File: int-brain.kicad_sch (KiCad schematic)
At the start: 52 parts, among them J1 PWR, J10 Left, J11 Right, J12 1MA_ENC, J13 1MB_ENC, J14 2MA_ENC, J15 2MB_ENC, J16 USB_A, J2 UART0, J3 I2C0, J4 PWR, J5 1MA, J6 1MB, J7 2MA, J8 2MB, J9 MPU9250, SW1 SW_Push, U2 ESP32-DevKitC, U7 PCA9635

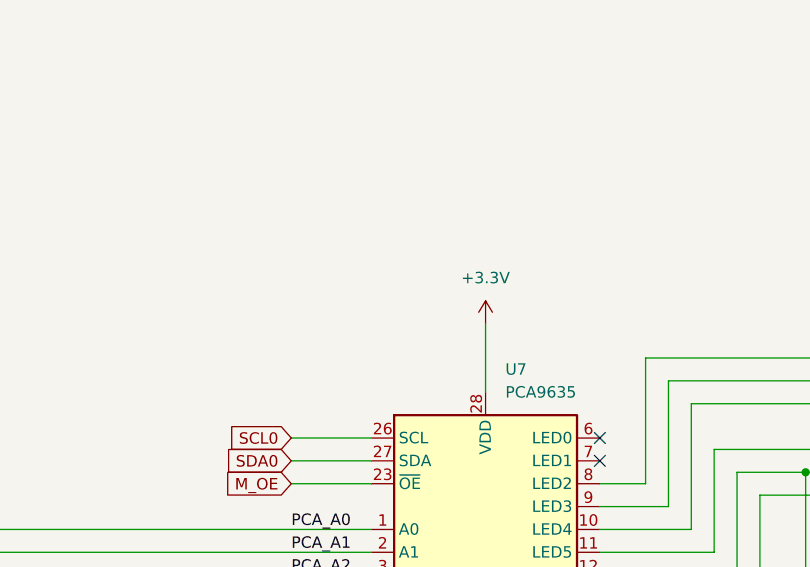
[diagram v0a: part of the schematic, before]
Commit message: add cap to PCA ic
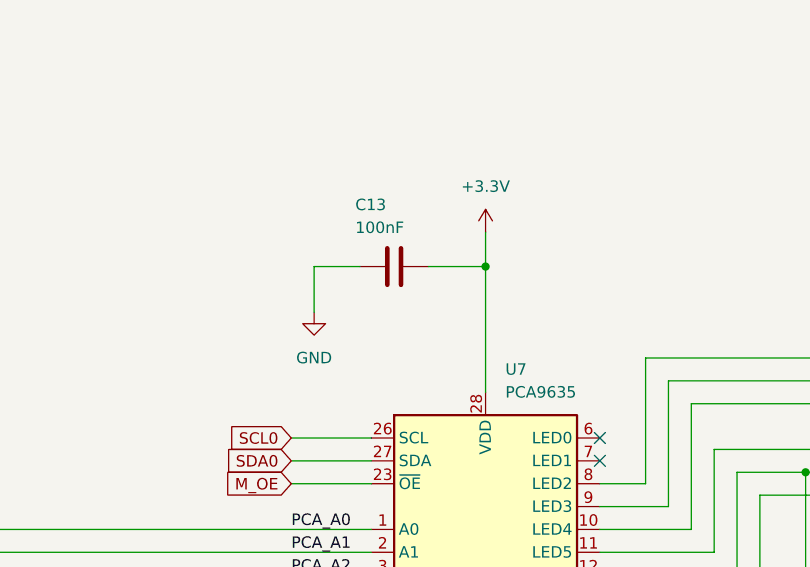
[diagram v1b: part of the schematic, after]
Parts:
- added C13: 100nF, Capacitor_SMD:C_0603_1608Metric_Pad1.08x0.95mm_HandSolder, symbol Device:C
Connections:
- net +3.3V: now also C13.1
- net GND: now also C13.2
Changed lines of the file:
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@@
 	)
 	(junction
+		(at 151.13 354.33)
+		(diameter 0)
+		(color 0 0 0 0)
+	)
+	(junction
 		(at 95.25 408.94)
 		(diameter 0)
@@
 	(wire
 		(pts
+			(xy 132.08 354.33) (xy 132.08 359.41)
+		)
+		(stroke
+			(width 0)
+			(type default)
+		)
+	)
+	(wire
+		(pts
 			(xy 328.93 158.75) (xy 328.93 146.05)
 		)
@@
 	(wire
 		(pts
+			(xy 137.16 354.33) (xy 132.08 354.33)
+		)
+		(stroke
+			(width 0)
+			(type default)
+		)
+	)
+	(wire
+		(pts
 			(xy 95.25 408.94) (xy 105.41 408.94)
 		)
@@
 	(wire
 		(pts
+			(xy 151.13 354.33) (xy 151.13 368.3)
+		)
+		(stroke
+			(width 0)
+			(type default)
+		)
+	)
+	(wire
+		(pts
 			(xy 81.28 224.79) (xy 81.28 271.78)
 		)
@@
 	(wire
 		(pts
+			(xy 144.78 354.33) (xy 151.13 354.33)
+		)
+		(stroke
+			(width 0)
+			(type default)
+		)
+	)
+	(wire
+		(pts
 			(xy 38.1 367.03) (xy 40.64 367.03)
 		)
@@
 	(wire
 		(pts
-			(xy 151.13 360.68) (xy 151.13 368.3)
+			(xy 151.13 350.52) (xy 151.13 354.33)
 		)
 		(stroke
@@
 	)
 	(symbol
+		(lib_id "Device:C")
+		(at 140.97 354.33 270)
+		(unit 1)
+		(exclude_from_sim no)
+		(in_bom yes)
+		(on_board yes)
+		(dnp no)
+		(property "Reference" "C13"
+			(at 136.652 347.472 90)
+			(effects
+				(font
+					(size 1.27 1.27)
+				)
+				(justify left)
+			)
+		)
+		(property "Value" "100nF"
+			(at 136.652 350.012 90)
+			(effects
+				(font
+					(size 1.27 1.27)
+				)
+				(justify left)
+			)
+		)
+		(property "Footprint" "Capacitor_SMD:C_0603_1608Metric_Pad1.08x0.95mm_HandSolder"
+			(at 137.16 355.2952 0)
+			(effects
+				(font
+					(size 1.27 1.27)
+				)
+				(hide yes)
+			)
+		)
+		(property "Datasheet" "~"
+			(at 140.97 354.33 0)
+			(effects
+				(font
+					(size 1.27 1.27)
+				)
+				(hide yes)
+			)
+		)
+		(property "Description" "Unpolarized capacitor"
+			(at 140.97 354.33 0)
+			(effects
+				(font
+					(size 1.27 1.27)
+				)
+				(hide yes)
+			)
+		)
+		(pin "2"
+		)
+		(pin "1"
+		)
+		(instances
+			(project "int-brain"
+				(path "/177c6115-ec2a-43b1-88e2-eca3e5dd1279"
+					(reference "C13")
+					(unit 1)
+				)
+			)
+		)
+	)
+	(symbol
 		(lib_id "Jumper:SolderJumper_2_Open")
 		(at 44.45 393.7 0)
@@
 	)
 	(symbol
+		(lib_id "power:GND")
+		(at 132.08 359.41 0)
+		(unit 1)
+		(exclude_from_sim no)
+		(in_bom yes)
+		(on_board yes)
+		(dnp no)
+		(fields_autoplaced yes)
+		(property "Reference" "#PWR030"
+			(at 132.08 365.76 0)
+			(effects
+				(font
+					(size 1.27 1.27)
+				)
+				(hide yes)
+			)
+		)
+		(property "Value" "GND"
+			(at 132.08 364.49 0)
+			(effects
+				(font
+					(size 1.27 1.27)
+				)
+			)
+		)
+		(property "Footprint" ""
+			(at 132.08 359.41 0)
+			(effects
+				(font
+					(size 1.27 1.27)
+				)
+				(hide yes)
+			)
+		)
+		(property "Datasheet" ""
+			(at 132.08 359.41 0)
+			(effects
+				(font
+					(size 1.27 1.27)
+				)
+				(hide yes)
+			)
+		)
+		(property "Description" "Power symbol creates a global label with name \"GND\" , ground"
+			(at 132.08 359.41 0)
+			(effects
+				(font
+					(size 1.27 1.27)
+				)
+				(hide yes)
+			)
+		)
+		(pin "1"
+		)
+		(instances
+			(project "int-brain"
+				(path "/177c6115-ec2a-43b1-88e2-eca3e5dd1279"
+					(reference "#PWR030")
+					(unit 1)
+				)
+			)
+		)
+	)
+	(symbol
 		(lib_id "power:+3.3V")
-		(at 151.13 360.68 0)
+		(at 151.13 350.52 0)
 		(unit 1)
 		(exclude_from_sim no)
@@
 		(fields_autoplaced yes)
 		(property "Reference" "#PWR039"
-			(at 151.13 364.49 0)
+			(at 151.13 354.33 0)
 			(effects
 				(font
@@
 		)
 		(property "Value" "+3.3V"
-			(at 151.13 355.6 0)
+			(at 151.13 345.44 0)
 			(effects
 				(font
@@
 		)
 		(property "Footprint" ""
-			(at 151.13 360.68 0)
+			(at 151.13 350.52 0)
 			(effects
 				(font
@@
 		)
 		(property "Datasheet" ""
-			(at 151.13 360.68 0)
+			(at 151.13 350.52 0)
 			(effects
 				(font
@@
 		)
 		(property "Description" "Power symbol creates a global label with name \"+3.3V\""
-			(at 151.13 360.68 0)
+			(at 151.13 350.52 0)
 			(effects
 				(font

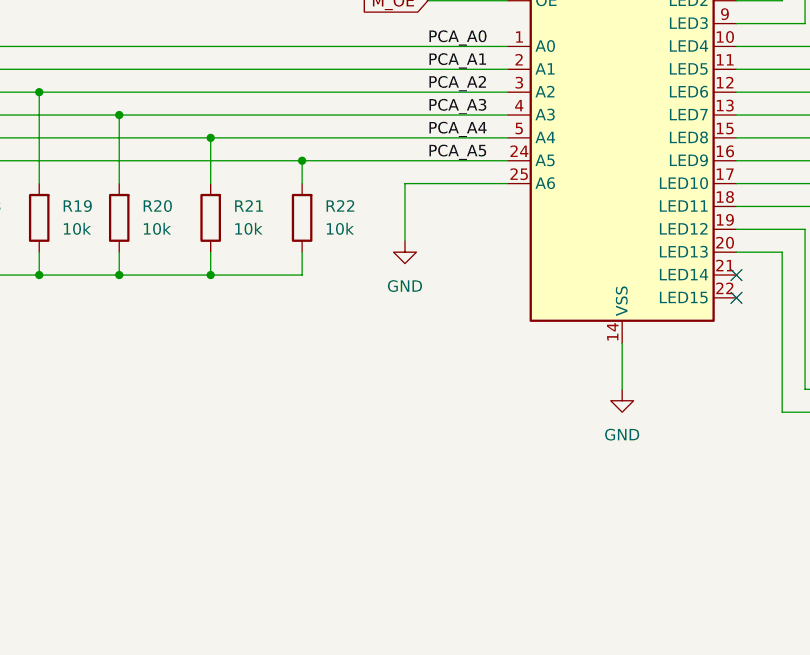
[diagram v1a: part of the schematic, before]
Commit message: add solder point for PCA I/O
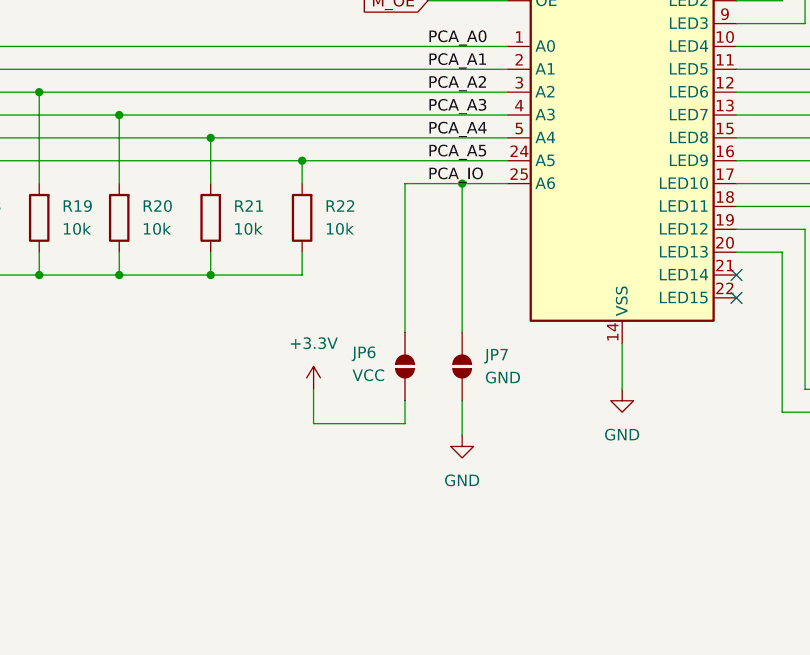
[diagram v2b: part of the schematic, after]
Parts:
- added JP6: VCC, Jumper:SolderJumper-2_P1.3mm_Open_Pad1.0x1.5mm, symbol Jumper:SolderJumper_2_Open
- added JP7: GND, Jumper:SolderJumper-2_P1.3mm_Open_Pad1.0x1.5mm, symbol Jumper:SolderJumper_2_Open
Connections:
- net +3.3V: now also JP6.1 (A)
- net GND: now also JP7.1 (A); no longer U7.25 (A6)
- new net PCA_IO: JP6.2 (B), JP7.2 (B), U7.25 (A6)

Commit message: placed?
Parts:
- removed JP7: GND, Jumper:SolderJumper-2_P1.3mm_Open_Pad1.0x1.5mm, symbol Jumper:SolderJumper_2_Open
- added D10: D, Diode_SMD:D_SMA_Handsoldering, symbol Device:D
- added J17: Conn_01x03, Connector_PinHeader_2.54mm:PinHeader_1x03_P2.54mm_Vertical, symbol Connector_Generic:Conn_01x03
- added R29: 10k, Resistor_SMD:R_1206_3216Metric_Pad1.30x1.75mm_HandSolder, symbol Device:R
- added R30: 3k9, Resistor_SMD:R_1206_3216Metric_Pad1.30x1.75mm_HandSolder, symbol Device:R
- D1: renamed from D18; footprint LED_SMD:LED_0603_1608Metric_Pad1.05x0.95mm_HandSolder -> LED_SMD:LED_1206_3216Metric_Pad1.42x1.75mm_HandSolder
- D2: renamed from D19; footprint LED_SMD:LED_0603_1608Metric_Pad1.05x0.95mm_HandSolder -> LED_SMD:LED_1206_3216Metric_Pad1.42x1.75mm_HandSolder
- D3: renamed from D20; footprint LED_SMD:LED_0603_1608Metric_Pad1.05x0.95mm_HandSolder -> LED_SMD:LED_1206_3216Metric_Pad1.42x1.75mm_HandSolder
- D4: renamed from D21; footprint LED_SMD:LED_0603_1608Metric_Pad1.05x0.95mm_HandSolder -> LED_SMD:LED_1206_3216Metric_Pad1.42x1.75mm_HandSolder
- D6: renamed from D25; footprint LED_SMD:LED_0603_1608Metric_Pad1.05x0.95mm_HandSolder -> LED_SMD:LED_1206_3216Metric_Pad1.42x1.75mm_HandSolder
- D7: renamed from D22; footprint LED_SMD:LED_0603_1608Metric_Pad1.05x0.95mm_HandSolder -> LED_SMD:LED_1206_3216Metric_Pad1.42x1.75mm_HandSolder
- R10: renamed from R11; value 10k -> 3k9
- U2: footprint PCM_Espressif:ESP32-DevKitC -> PCM_Espressif:ESP32-DevKitC-slim
- renumbered C13 to C1, D23 to D5, J11 to J1, J8 to J10, J6 to J11, J5 to J12, J12 to J13, J13 to J14, J14 to J15, J9 to J16, J10 to J2, J1 to J3, J16 to J5, J15 to J6, J3 to J7, J2 to J8, J7 to J9, JP0 to JP1, JP1 to JP2, JP2 to JP3, JP3 to JP4, JP4 to JP5, JP5 to JP6, JP6 to JP7, R5 to R1, R21 to R11, R22 to R12, R23 to R13, R9 to R14, R16 to R15, R17 to R16, R6 to R2, R7 to R3, R28 to R4, R8 to R5, R18 to R6, R19 to R7, R10 to R8, R20 to R9, U7 to U1
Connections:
- net 1MA_EN: now also U1.22 (LED15); no longer U1.12 (LED6)
- net 1MB_EN: now also U1.21 (LED14); no longer U1.9 (LED3)
- net 2MA_EN: now also U1.6 (LED0); no longer U1.16 (LED9)
- net 2MB_EN: now also U1.7 (LED1); no longer U1.19 (LED12)
- net BUCK_VS: no longer D5.1 (K)
- net GND: now also J3.3 (MountPin), R29.1, R30.2; no longer J3.MP (MountPin)
- net PCA_IO: now also R29.2
- net VBATT: now also J17.2 (Pin_2); no longer R10.1
- net VS: now also D5.1 (K), D10.1 (K); no longer D5.2 (A), J3.1, J4.2 (Pin_2)
- net 1MA1_IN renamed 2MB_IN2
- net 1MA2_IN renamed 2MA_IN2
- net 1MB1_IN renamed 2MA_IN1
- net 1MB2_IN: no longer names the net of U1.8 (LED2)
- net 2MA1_IN renamed 1MB_IN1
- net 2MA2_IN renamed 1MA_IN1
- net 2MB1_IN renamed 1MA_IN2
- net 2MB2_IN: no longer names the net of U1.20 (LED13)
- new net 1MB_IN2: U1.16 (LED9)
- new net 2MB_IN1: U1.12 (LED6)
- new net 3S: J17.3 (Pin_3), R10.1
- new net 6S: J17.1 (Pin_1), R30.1
- new net VS_UNSAFE: D10.2 (A), D5.2 (A), J3.1, J4.2 (Pin_2)
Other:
- removed sheet motor_driver_1
- removed sheet motor_driver_2
- added sheet motor-driver-1 (motor-driver-DRV8251A.kicad_sch)
- added sheet motor-driver-2 (motor-driver-DRV8251A.kicad_sch)
- added sheet motor-driver-3 (motor-driver-DRV8251A.kicad_sch)
- added sheet motor-driver-4 (motor-driver-DRV8251A.kicad_sch)
- moved on the sheet: D1, D2, D3, D4, D5, J10, J11, J12, J3, J4, J9, R1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

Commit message: traced
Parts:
- added C26, C27: 10uF, Capacitor_SMD:C_1206_3216Metric_Pad1.33x1.80mm_HandSolder, symbol Device:C
- added U13: AMS1117-3.3, Package_TO_SOT_SMD:SOT-223-3_TabPin2, symbol Regulator_Linear:AMS1117-3.3
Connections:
- net BUCK_VS is gone; now on net VS: SW1.1
- net GPIO32 is gone; now on net FSYNC: J2.7 (Pin_7), U2.7 (32K_XP/GPIO32/ADC1_CH4)
- net GPIO33 is gone; now on net INT: J2.8 (Pin_8), U2.8 (32K_XN/GPIO33/ADC1_CH5)
- net +3.3V: now also C27.1, U13.2 (VO); no longer J2.1 (Pin_1), U2.1 (3V3)
- net 1MA1_ENC: now also J1.9 (Pin_9), U2.30 (GPIO18); no longer J1.11 (Pin_11), U2.28 (GPIO17)
- net 1MA2_ENC: now also J1.8 (Pin_8), U2.31 (GPIO19); no longer J1.10 (Pin_10), U2.29 (GPIO5)
- net 1MA_EN: now also U1.18 (LED11); no longer U1.22 (LED15)
- net 1MA_IN1: now also U1.19 (LED12); no longer U1.17 (LED10)
- net 1MA_IN2: now also U1.20 (LED13); no longer U1.18 (LED11)
- net 1MB1_ENC: now also J2.11 (Pin_11), U2.11 (ADC2_CH7/GPIO27); no longer J2.12 (Pin_12), U2.12 (MTMS/GPIO14/ADC2_CH6)
- net 1MB2_ENC: now also J2.10 (Pin_10), U2.10 (DAC_2/ADC2_CH9/GPIO26); no longer J2.13 (Pin_13), U2.13 (MTDI/GPIO12/ADC2_CH5)
- net 1MB_EN: now also U1.17 (LED10); no longer U1.21 (LED14)
- net 2MA1_ENC: now also J1.10 (Pin_10), U2.29 (GPIO5); no longer J1.8 (Pin_8), U2.31 (GPIO19)
- net 2MA2_ENC: now also J1.11 (Pin_11), U2.28 (GPIO17); no longer J1.9 (Pin_9), U2.30 (GPIO18)
- net 2MA_EN: now also U1.8 (LED2); no longer U1.6 (LED0)
- net 2MA_IN1: now also U1.9 (LED3); no longer U1.10 (LED4)
- net 2MA_IN2: now also U1.10 (LED4); no longer U1.11 (LED5)
- net 2MB1_ENC: now also J2.12 (Pin_12), U2.12 (MTMS/GPIO14/ADC2_CH6); no longer J2.10 (Pin_10), U2.10 (DAC_2/ADC2_CH9/GPIO26)
- net 2MB2_ENC: now also J2.13 (Pin_13), U2.13 (MTDI/GPIO12/ADC2_CH5); no longer J2.11 (Pin_11), U2.11 (ADC2_CH7/GPIO27)
- net 2MB_EN: now also U1.13 (LED7); no longer U1.7 (LED1)
- net 2MB_IN1: now also U1.11 (LED5); no longer U1.12 (LED6)
- net 2MB_IN2: now also U1.12 (LED6); no longer U1.13 (LED7)
- net FSYNC: no longer J1.2 (Pin_2), U2.37 (GPIO23)
- net GND: now also C26.2, C27.2, U13.1 (GND)
- net INT: no longer J1.12 (Pin_12), U2.27 (GPIO16)
- net VSS: now also C26.1, U13.3 (VI)
- new net +3.3VA: J2.1 (Pin_1), U2.1 (3V3)
- new net GPIO16: J1.12 (Pin_12), U2.27 (GPIO16)
- new net GPIO23: J1.2 (Pin_2), U2.37 (GPIO23)
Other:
- moved on the sheet: J15, J6

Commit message: done?
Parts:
- added R31: 10k, Resistor_SMD:R_1206_3216Metric_Pad1.30x1.75mm_HandSolder, symbol Device:R
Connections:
- net +3.3V: now also R31.2
- net M_OE: now also R31.1
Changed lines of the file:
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@@
 	)
 	(junction
+		(at 114.3 354.33)
+		(diameter 0)
+		(color 0 0 0 0)
+	)
+	(junction
 		(at 132.08 463.55)
 		(diameter 0)
@@
 	(wire
 		(pts
+			(xy 114.3 354.33) (xy 114.3 378.46)
+		)
+		(stroke
+			(width 0)
+			(type default)
+		)
+	)
+	(wire
+		(pts
 			(xy 298.45 439.42) (xy 317.5 439.42)
 		)
@@
 	(wire
 		(pts
+			(xy 114.3 336.55) (xy 114.3 342.9)
+		)
+		(stroke
+			(width 0)
+			(type default)
+		)
+	)
+	(wire
+		(pts
 			(xy 50.8 209.55) (xy 97.79 209.55)
 		)
@@
 	(wire
 		(pts
+			(xy 114.3 350.52) (xy 114.3 354.33)
+		)
+		(stroke
+			(width 0)
+			(type default)
+		)
+	)
+	(wire
+		(pts
 			(xy 328.93 163.83) (xy 328.93 158.75)
 		)
@@
 	(wire
 		(pts
-			(xy 129.54 378.46) (xy 138.43 378.46)
+			(xy 105.41 354.33) (xy 114.3 354.33)
 		)
 		(stroke
@@
 	(wire
 		(pts
+			(xy 114.3 378.46) (xy 138.43 378.46)
+		)
+		(stroke
+			(width 0)
+			(type default)
+		)
+	)
+	(wire
+		(pts
 			(xy 322.58 143.51) (xy 322.58 156.21)
 		)
@@
 	(global_label "M_OE"
 		(shape input)
-		(at 129.54 378.46 180)
+		(at 105.41 354.33 180)
 		(fields_autoplaced yes)
 		(effects
@@
 		)
 		(property "Intersheetrefs" "${INTERSHEET_REFS}"
-			(at 121.6563 378.46 0)
+			(at 97.5263 354.33 0)
 			(effects
 				(font
@@
 	)
 	(symbol
+		(lib_id "power:+3.3V")
+		(at 114.3 336.55 0)
+		(unit 1)
+		(exclude_from_sim no)
+		(in_bom yes)
+		(on_board yes)
+		(dnp no)
+		(fields_autoplaced yes)
+		(property "Reference" "#PWR059"
+			(at 114.3 340.36 0)
+			(effects
+				(font
+					(size 1.27 1.27)
+				)
+				(hide yes)
+			)
+		)
+		(property "Value" "+3.3V"
+			(at 114.3 331.47 0)
+			(effects
+				(font
+					(size 1.27 1.27)
+				)
+			)
+		)
+		(property "Footprint" ""
+			(at 114.3 336.55 0)
+			(effects
+				(font
+					(size 1.27 1.27)
+				)
+				(hide yes)
+			)
+		)
+		(property "Datasheet" ""
+			(at 114.3 336.55 0)
+			(effects
+				(font
+					(size 1.27 1.27)
+				)
+				(hide yes)
+			)
+		)
+		(property "Description" "Power symbol creates a global label with name \"+3.3V\""
+			(at 114.3 336.55 0)
+			(effects
+				(font
+					(size 1.27 1.27)
+				)
+				(hide yes)
+			)
+		)
+		(pin "1"
+		)
+		(instances
+			(project "int-brain"
+				(path "/177c6115-ec2a-43b1-88e2-eca3e5dd1279"
+					(reference "#PWR059")
+					(unit 1)
+				)
+			)
+		)
+	)
+	(symbol
 		(lib_id "Jumper:SolderJumper_2_Open")
 		(at 44.45 375.92 0)
@@
 					(unit 1)
 				)
+			)
+		)
+	)
+	(symbol
+		(lib_id "Device:R")
+		(at 114.3 346.71 180)
+		(unit 1)
+		(exclude_from_sim no)
+		(in_bom yes)
+		(on_board yes)
+		(dnp no)
+		(fields_autoplaced yes)
+		(property "Reference" "R31"
+			(at 116.84 345.4399 0)
+			(effects
+				(font
+					(size 1.27 1.27)
+				)
+				(justify right)
+			)
+		)
+		(property "Value" "10k"
+			(at 116.84 347.9799 0)
+			(effects
+				(font
+					(size 1.27 1.27)
+				)
+				(justify right)
+			)
+		)
+		(property "Footprint" "Resistor_SMD:R_1206_3216Metric_Pad1.30x1.75mm_HandSolder"
+			(at 116.078 346.71 90)
+			(effects
+				(font
+					(size 1.27 1.27)
+				)
+				(hide yes)
+			)
+		)
+		(property "Datasheet" "~"
+			(at 114.3 346.71 0)
+			(effects
+				(font
+					(size 1.27 1.27)
+				)
+				(hide yes)
+			)
+		)
+		(property "Description" "Resistor"
+			(at 114.3 346.71 0)
+			(effects
+				(font
+					(size 1.27 1.27)
+				)
+				(hide yes)
+			)
+		)
+		(pin "2"
+		)
+		(pin "1"
+		)
+		(instances
+			(project "int-brain"
+				(path "/177c6115-ec2a-43b1-88e2-eca3e5dd1279"
+					(reference "R31")
+					(unit 1)
+				)

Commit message: minor improvements
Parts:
- D10, D5: value D -> M7
- J1: value Right -> Top
- J17: value Conn_01x03 -> VBATT_SELECT
- J2: value Left -> Bottom
- JP7: value VCC -> I/O
- R30: value 3k9 -> 2k
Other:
- note added: "3.3V LDO"
- note added: "Default I/O to output mode by pull-down."
- note added: "Distriute functionality from the ESP32 to the rest of the board. In general, the signal bus is used to connect headers on either side of the board to access its GPIO and other functionality. Nothing else on the board depends on ESP32 3.3V, so this can be used for peripherals."
- note added: "Drive all motors using PWM signals, sent from the ESP32 using I2C. Eachmotor requires two PWM lines, each corresponding to one pair of the MOSFETs in the H-bridge motor driver. An additional PWM pin has been allocated per motor to indicate speed with LED brightness."
- note added: "ESP32 Microcontroller"
- note added: "I2C address selection is done by pulling down all bits to 0 using a 10k resistor to ground. To make any of them 1, the corresponding solder joint can be filled, and they'll be shorted to 3.3 V."
- note added: "MPU9250 Datasheet: https://invensense.tdk.com/wp-content/uploads/2015/02/ PS-MPU-9250A-01-v1.1.pdf"
- note added: "Motor Logic Section"
- note added: "Note that this +3.3VA is different from the +3.3V used in the rest of the circuit. This is to ensure that the 3.3 V required for the ESP32 is left undisturbed and other components are powered using a dedicated AMS1117-3.3 LDO."
- note added: "PCA9635 datasheet: https://www.nxp.com/docs/en/data-sheet/PCA9635.pdf"
- note added: "Pinout and other information: https://docs.espressif.com/projects/esp-idf/en/stable/esp32/ hw-reference/esp32/get-started-devkitc.html"
- note added: "Power Input Section"
- note added: "Protocol pins (I2C and UART0) are chosen to keep compliance with the Arduino framework, even though this is unlikely to be used with this board. Most other GPIO are chosen based on physical proximity to peripherals and ease of routing the PCB."
- note added: "Provide up to 5V 5A at a USB port, used to drive an SBC such as the Raspberry Pi 5B"
- note added: "SBC Power section"
- note added: "Sensor Module product links - https://robu.in/product/gy-9255-mpu9255-sensor-module/ - https://www.electronicscomp.com/mpu9250-9-axis-gyro- accelerometer-module - https://www.amazon.in/Electrobot-MPU9250-Accelerator- Magnetometer-Arduino/dp/B08R3SXRVH - https://roboticsdna.in/product/gy-87-mpu-9265-3-axis-9-dof- attitude-gyro-magnetometer-accelerator-sensor-module/ - https://rees52.com/products/m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"
- note added: "Support for quadrature rotary encoders is added, in case a compatible motor with encoders can be found. These are connected directly to the ESP32 microcontroller (instead of using another PCA PWM driver) to provide easy configration of hardware interrupts in case this approach is used when programming for the encoders. One JST header for each encoder (one per motor)."
- note added: "Symbol and footprint libraries: https://github.com/espressif/kicad-libraries"
- note added: "Take in 12 V or 24 V (approx; for most calculations, peak values assuming lithium-polymer cells at 4.2 V are considered). Provide basic reverse-polarity protection (diodes) and also reduce to 5V for most of the board's functionality. Provide a voltage reading corresponding to the battery leverl for the microcontroller too."
- note added: "The PCA driver has an active-low enable, so we pull-up to 3.3 V (high) to prevent accidental activation."
- note added: "These ADC pins can only handle input, so they are used for current-sense voltage drops."
- note added: "Use a potential divider to reduce the battery voltage. For various Li-Po batteries, we assume 4.2 V per cell (at full charge). We expect about 3.12 mW - 12.96 mW to be dissipated here. 3S: 47k and 3.9k --> 0.9654223 V 6S: 47k and 2k --> 1.028571429 V The ESP32 seems to read realiably up to around 1 V using the built-in ADCs."
- company: (none) -> Anuj Verma
- title: (none) -> RoboNex
- moved on the sheet: C1, C26, C27, D1, D10, D2, D3, D4, D5, D6, D7, H1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

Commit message: link to README
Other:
- note added: "Find chosen pinouts in the README: https://github.com/eccentricOrange/int-brain/blob/ main/README.md"
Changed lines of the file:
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@@
+		)
+	)
+	(text "Find chosen pinouts in the README:\nhttps://github.com/eccentricOrange/int-brain/blob/\nmain/README.md"
+		(exclude_from_sim no)
+		(at 33.528 52.578 0)
+		(effects
+			(font
+				(size 1.27 1.27)
+			)
+			(justify left)
+			(href "https://github.com/eccentricOrange/int-brain/blob/main/README.md")
 		)
 	)
